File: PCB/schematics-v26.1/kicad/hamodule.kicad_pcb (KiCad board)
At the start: 4 copper layers, 131.1 x 83.7 mm, 206 parts, among them J1 GND|5V, J10 Tx|Rx, J11 Sda|Scl, J12 3|9, J13 13|12, J14 3.3v|GND|7|15, J15 2604-1104, J16 2604-1104, J17 TestPoint, J19 TestPoint, J2 2604-1102, J3 USB_C_Receptacle_USB2.0, J4 GND|3.3V, J5 Jumper 3.3v, J6 2604-1104, J7 2604-1104, J8 5v|GND|Do, J9 Screen, K1 AQG22205, K2 AQG22205, K3 AQG22205, K4 AQG22205, K5 AQG22205, K6 AQG22205, K7 AQG22205, K8 AQG22205, SW1 USB | PS, SW2 Reset, SW3 Boot, U1 LD1117AV33, U10 SN74LV1T34DBV, U11 ULN2803A, U12 TCAL6416, U14 74AHC1G04, U2 USBLC6-2SC6, U3 ESP32-S3-WROOM-2, U4 LDA210, U5 LDA210, U6 LDA210, U7 LDA210, U8 SHT4x, U9 SN74LVCH8T245

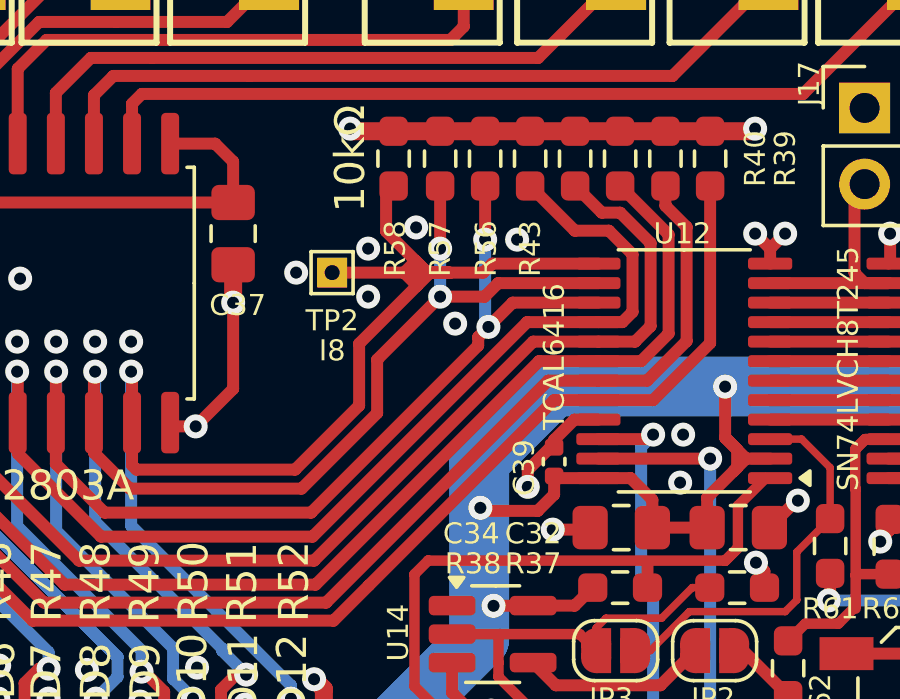
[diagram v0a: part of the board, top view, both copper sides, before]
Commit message: moved a bit the data lines between TCAL and SNT to make sure they have solid GND plane beneath. Updated footprints from library since Kibot complains. lets see if it fixes it
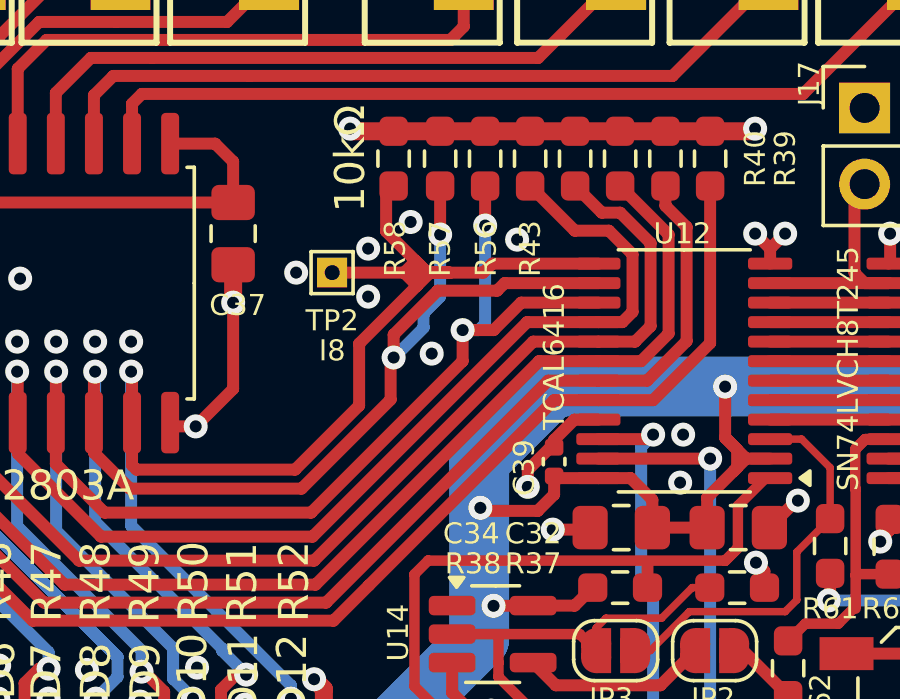
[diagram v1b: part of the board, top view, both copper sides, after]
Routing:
- net Net-(U11-I7): track 43.0 -> 45.8 mm
- net Net-(U11-I6): track 43.6 -> 44.7 mm
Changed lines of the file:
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@@
 		(tags "CP Radial series Radial pin pitch 2.50mm diameter 6.3mm height 7mm Electrolytic Capacitor")
 		(property "Reference" "C12"
-			(at 4.582379 2.6 180)
+			(at 4.582379 2.6 0)
 			(layer "F.SilkS")
 			(effects
@@
 	)
 	(via
-		(at 75.2 86.294307)
+		(at 75.017347 86.111653)
 		(size 0.8)
 		(drill 0.4)
@@
 	)
 	(via
-		(at 76.5 89.5)
+		(at 75.719269 90.499269)
 		(size 0.8)
 		(drill 0.4)
@@
 	)
 	(segment
+		(start 78.15 88.15)
+		(end 81.275 88.15)
+		(width 0.4)
+		(layer "F.Cu")
+		(net 168)
+	)
+	(segment
 		(start 64.46 92.8)
 		(end 64.46 91.14)
@@
 	)
 	(segment
-		(start 73.901 92.481786)
-		(end 71.382786 95)
+		(start 75.916156 88.402)
+		(end 77.898 88.402)
 		(width 0.4)
 		(layer "F.Cu")
@@
 	)
 	(segment
-		(start 64.46 93.799999)
-		(end 64.46 92.925)
+		(start 65.660001 95)
+		(end 64.46 93.799999)
 		(width 0.4)
 		(layer "F.Cu")
@@
 	)
 	(segment
-		(start 76 87)
-		(end 76 84.9125)
+		(start 69.199395 101.200605)
+		(end 69.533773 101.200605)
 		(width 0.4)
 		(layer "F.Cu")
@@
 	)
 	(segment
-		(start 77.935784 88.15)
-		(end 81.275 88.15)
+		(start 64.46 93.799999)
+		(end 64.46 92.925)
 		(width 0.4)
 		(layer "F.Cu")
@@
 	)
 	(segment
-		(start 76 88.601)
-		(end 73.901 90.7)
+		(start 74.45 90.63)
+		(end 74.45 89.868156)
 		(width 0.4)
 		(layer "F.Cu")
@@
 	)
 	(segment
-		(start 69.199395 101.200605)
-		(end 69.533773 101.200605)
+		(start 68.698 101.702)
+		(end 69.199395 101.200605)
 		(width 0.4)
 		(layer "F.Cu")
@@
 	)
 	(segment
-		(start 77.484784 88.601)
-		(end 77.935784 88.15)
+		(start 74.45 89.868156)
+		(end 75.916156 88.402)
 		(width 0.4)
 		(layer "F.Cu")
@@
 	)
 	(segment
-		(start 68.698 101.702)
-		(end 69.199395 101.200605)
+		(start 68.698 102.974004)
+		(end 68.698 101.702)
 		(width 0.4)
 		(layer "F.Cu")
@@
 	)
 	(segment
-		(start 65.660001 95)
-		(end 64.46 93.799999)
+		(start 69.4 103.676004)
+		(end 68.698 102.974004)
 		(width 0.4)
 		(layer "F.Cu")
@@
 	)
 	(segment
-		(start 68.698 102.974004)
-		(end 68.698 101.702)
+		(start 74.35 92.032786)
+		(end 71.382786 95)
 		(width 0.4)
 		(layer "F.Cu")
@@
 	)
 	(segment
-		(start 69.4 103.676004)
-		(end 68.698 102.974004)
+		(start 74.45 90.63)
+		(end 74.35 90.73)
 		(width 0.4)
 		(layer "F.Cu")
@@
 	)
 	(segment
-		(start 73.901 90.7)
-		(end 73.901 92.481786)
+		(start 76 86.53)
+		(end 76 84.9125)
 		(width 0.4)
 		(layer "F.Cu")
@@
 	)
 	(segment
-		(start 76 88.601)
-		(end 77.484784 88.601)
+		(start 74.35 90.73)
+		(end 74.35 92.032786)
 		(width 0.4)
 		(layer "F.Cu")
@@
 	)
 	(segment
-		(start 71.382786 95)
-		(end 65.660001 95)
+		(start 77.898 88.402)
+		(end 78.15 88.15)
 		(width 0.4)
 		(layer "F.Cu")
@@
 		(net 168)
 	)
+	(segment
+		(start 71.382786 95)
+		(end 65.660001 95)
+		(width 0.4)
+		(layer "F.Cu")
+		(net 168)
+	)
 	(via
 		(at 64.5 91.1)
@@
 	)
 	(via
-		(at 76 87)
+		(at 76 86.53)
 		(size 0.8)
 		(drill 0.4)
@@
 	)
 	(via
-		(at 76 88.601)
+		(at 74.45 90.63)
 		(size 0.8)
 		(drill 0.4)
@@
 	)
 	(segment
-		(start 76 88.601)
-		(end 76 87)
+		(start 68.731478 100.331478)
+		(end 64.5 96.1)
 		(width 0.4)
 		(layer "B.Cu")
@@
 	)
 	(segment
-		(start 68.731478 100.331478)
-		(end 64.5 96.1)
+		(start 74.457166 90.63)
+		(end 75.45 89.637166)
 		(width 0.4)
 		(layer "B.Cu")
@@
 	)
 	(segment
+		(start 75.45 89.637166)
+		(end 75.45 89.151)
+		(width 0.4)
+		(layer "B.Cu")
+		(net 168)
+	)
+	(segment
 		(start 64.5 96.1)
 		(end 64.5 91.1)
@@
 	)
 	(segment
-		(start 78.41857 88.8)
-		(end 81.275 88.8)
+		(start 74.45 90.63)
+		(end 74.457166 90.63)
+		(width 0.4)
+		(layer "B.Cu")
+		(net 168)
+	)
+	(segment
+		(start 76 88.601)
+		(end 76 86.53)
+		(width 0.4)
+		(layer "B.Cu")
+		(net 168)
+	)
+	(segment
+		(start 75.45 89.151)
+		(end 76 88.601)
+		(width 0.4)
+		(layer "B.Cu")
+		(net 168)
+	)
+	(segment
+		(start 63.19 94.174999)
+		(end 63.19 93.3)
 		(width 0.4)
 		(layer "F.Cu")
@@
 	)
 	(segment
-		(start 67.763 103.664604)
-		(end 67.7744 103.676004)
+		(start 76.75 89.715711)
+		(end 77.784289 89.715711)
 		(width 0.4)
 		(layer "F.Cu")
@@
 	)
 	(segment
-		(start 77.609285 89.609285)
-		(end 78.41857 88.8)
+		(start 71.7 95.8)
+		(end 64.815001 95.8)
 		(width 0.4)
 		(layer "F.Cu")
@@
 	)
 	(segment
-		(start 63.19 91.11)
-		(end 63.2 91.1)
+		(start 76.75 89.715711)
+		(end 76.75 90.75)
 		(width 0.4)
 		(layer "F.Cu")
@@
 	)
 	(segment
-		(start 64.815001 95.8)
-		(end 63.19 94.174999)
+		(start 77.784289 89.715711)
+		(end 78.7 88.8)
 		(width 0.4)
 		(layer "F.Cu")
@@
 	)
 	(segment
-		(start 63.19 94.174999)
-		(end 63.19 93.3)
+		(start 67.763 103.664604)
+		(end 67.7744 103.676004)
 		(width 0.4)
 		(layer "F.Cu")
@@
 	)
 	(segment
-		(start 71.7 95.8)
-		(end 64.815001 95.8)
+		(start 78.7 88.8)
+		(end 81.275 88.8)
 		(width 0.4)
 		(layer "F.Cu")
@@
 	)
 	(segment
-		(start 77.268426 89.950144)
-		(end 77.268426 90.231574)
+		(start 63.19 91.11)
+		(end 63.2 91.1)
 		(width 0.4)
 		(layer "F.Cu")
@@
 	)
 	(segment
-		(start 77.268426 90.231574)
-		(end 71.7 95.8)
+		(start 77.5 86.23)
+		(end 77.5 84.9125)
 		(width 0.4)
 		(layer "F.Cu")
@@
 	)
 	(segment
-		(start 77.5 86.7)
-		(end 77.5 84.9125)
+		(start 63.19 92.8)
+		(end 63.19 91.11)
 		(width 0.4)
 		(layer "F.Cu")
@@
 	)
 	(segment
-		(start 63.19 92.8)
-		(end 63.19 91.11)
+		(start 64.815001 95.8)
+		(end 63.19 94.174999)
 		(width 0.4)
 		(layer "F.Cu")
@@
 	)
 	(segment
-		(start 77.609285 89.609285)
-		(end 77.268426 89.950144)
+		(start 76.75 90.75)
+		(end 71.7 95.8)
 		(width 0.4)
 		(layer "F.Cu")
@@
 	)
 	(via
-		(at 77.609285 89.609285)
+		(at 76.75 89.715711)
 		(size 0.8)
 		(drill 0.4)
@@
 	)
 	(via
-		(at 77.5 86.7)
+		(at 77.5 86.23)
 		(size 0.8)
 		(drill 0.4)
@@
 	)
 	(segment
-		(start 67.098 100.316414)
-		(end 67.098 101.335)
+		(start 77.5 89.5)
+		(end 77.5 86.23)
 		(width 0.4)
 		(layer "B.Cu")
@@
 	)
 	(segment
-		(start 77.5 89.5)
-		(end 77.609285 89.609285)
+		(start 67.098 100.316414)
+		(end 67.098 101.335)
 		(width 0.4)
 		(layer "B.Cu")
@@
 	)
 	(segment
+		(start 76.75 89.715711)
+		(end 77.284289 89.715711)
+		(width 0.4)
+		(layer "B.Cu")
+		(net 169)
+	)
+	(segment
 		(start 65.840793 99.059207)
 		(end 67.098 100.316414)
@@
 	)
 	(segment
-		(start 77.5 86.7)
+		(start 77.284289 89.715711)
 		(end 77.5 89.5)
 		(width 0.4)

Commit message: Finished Size 1
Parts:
- moved H5 0.83 mm to (52.2, 104.6)
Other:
- board size 131.1 x 83.7 mm -> 131.9 x 84.5 mm
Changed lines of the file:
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@@
 	(footprint "MountingHole:MountingHole_3.2mm_M3_ISO14580_Pad"
 		(layer "F.Cu")
-		(at 52.25 103.8)
+		(at 52.25 104.63)
 		(descr "Mounting Hole 3.2mm, M3, generated by kicad-footprint-generator mountinghole.py")
 		(tags "mountinghole M3 ISO14580")
@@
 	)
 	(gr_line
-		(start 147.25 31.8)
-		(end 31.37071 31.8)
+		(start 147.05 31.03)
+		(end 31.391411 31.03)
 		(stroke
 			(width 0.05)
@@
 	)
 	(gr_line
-		(start 23.9 106.3)
-		(end 23.900001 40.4004)
+		(start 23.05 106.3)
+		(end 23.05 40.4004)
 		(stroke
 			(width 0.05)
@@
 	)
 	(gr_line
-		(start 31.199084 110.009939)
-		(end 31.200916 115.1)
+		(start 31.1518 109.900032)
+		(end 31.15 115.1)
 		(stroke
 			(width 0.05)
-			(type default)
+			(type solid)
 		)
 		(layer "Edge.Cuts")
 	)
 	(gr_line
-		(start 24.3 40.000401)
-		(end 28.0293 40.001612)
+		(start 23.449999 40.000401)
+		(end 28.048388 40.001617)
 		(stroke
 			(width 0.05)
@@
 	)
 	(gr_arc
-		(start 147.25 31.8)
-		(mid 147.391421 31.858579)
-		(end 147.45 32)
+		(start 147.05 31.03)
+		(mid 147.191421 31.088579)
+		(end 147.25 31.23)
 		(stroke
 			(width 0.05)
@@
 	)
 	(gr_line
-		(start 27.901832 106.600916)
-		(end 24.2 106.6)
+		(start 27.85 106.600916)
+		(end 23.35 106.6)
 		(stroke
 			(width 0.05)
@@
 	)
 	(gr_arc
-		(start 150.65 40)
-		(mid 148.387258 39.062742)
-		(end 147.45 36.8)
+		(start 150.45 40)
+		(mid 148.187258 39.062742)
+		(end 147.25 36.8)
 		(stroke
 			(width 0.05)
@@
 	)
 	(gr_arc
-		(start 23.900001 40.4004)
-		(mid 24.017158 40.117558)
-		(end 24.3 40.000401)
+		(start 23.05 40.4004)
+		(mid 23.167157 40.117558)
+		(end 23.449999 40.000401)
 		(stroke
 			(width 0.05)
@@
 	)
 	(gr_arc
-		(start 31.130912 36.9)
-		(mid 30.222471 39.093171)
-		(end 28.0293 40.001612)
+		(start 31.15 36.9)
+		(mid 30.241559 39.093171)
+		(end 28.048388 40.001612)
 		(stroke
 			(width 0.05)
@@
 	)
 	(gr_line
-		(start 31.13 36.9)
-		(end 31.13 32.0414)
+		(start 31.15 36.9)
+		(end 31.15 31.271411)
 		(stroke
 			(width 0.05)
@@
 	)
 	(gr_line
-		(start 150.65 40)
+		(start 150.45 40)
 		(end 154.8 40)
 		(stroke
@@
 	)
 	(gr_line
-		(start 147.45 36.8)
-		(end 147.45 32)
+		(start 147.25 36.8)
+		(end 147.25 31.23)
 		(stroke
 			(width 0.05)
@@
 	)
 	(gr_arc
-		(start 24.2 106.6)
-		(mid 23.987868 106.512132)
-		(end 23.9 106.3)
+		(start 23.35 106.6)
+		(mid 23.137868 106.512132)
+		(end 23.05 106.3)
 		(stroke
 			(width 0.05)
@@
 	)
 	(gr_arc
-		(start 31.6 115.5)
-		(mid 31.317157 115.382843)
-		(end 31.2 115.1)
+		(start 31.55 115.5)
+		(mid 31.267157 115.382843)
+		(end 31.15 115.1)
 		(stroke
 			(width 0.05)
@@
 	)
 	(gr_arc
-		(start 27.901832 106.600916)
-		(mid 30.273186 107.606395)
-		(end 31.199084 110.009939)
+		(start 27.852748 106.600916)
+		(mid 30.185543 107.567218)
+		(end 31.1518 109.900032)
 		(stroke
 			(width 0.05)
-			(type default)
+			(type solid)
 		)
 		(layer "Edge.Cuts")
@@
 	(gr_line
 		(start 134.0866 115.5)
-		(end 31.6 115.5)
+		(end 31.55 115.5)
 		(stroke
 			(width 0.05)
@@
 	)
 	(gr_arc
-		(start 31.129289 32.0414)
-		(mid 31.199997 31.870697)
-		(end 31.3707 31.799989)
+		(start 31.15 31.271411)
+		(mid 31.220708 31.100708)
+		(end 31.391411 31.03)
 		(stroke
 			(width 0.05)
@@
 		(layer "Dwgs.User")
 		(pts
-			(xy 31.6 115.5) (xy 31.368396 31.8)
+			(xy 31.6 115.5) (xy 31.45 31.03)
 		)
 		(height -17.498728)
@@
 			(keep_text_aligned yes)
 		)
-		(gr_text "83.7003 mm"
-			(at 15.135533 73.695238 -89.84145881)
+		(gr_text "84.4701 mm"
+			(at 15.176298 73.294032 -89.8982555)
 			(layer "Dwgs.User")
 			(effects
@@
 		(layer "Dwgs.User")
 		(pts
-			(xy 147.8 31.8) (xy 147.8 40)
+			(xy 147.05 31.03) (xy 147.05 40.03)
 		)
 		(height -10.5)
@@
 			(keep_text_aligned yes)
 		)
-		(gr_text "8.2000 mm"
-			(at 157.15 35.9 90)
+		(gr_text "9.0000 mm"
+			(at 156.399984 35.529993 90)
 			(layer "Dwgs.User")
 			(effects
@@
 		(layer "Dwgs.User")
 		(pts
-			(xy 23.9 106.6) (xy 23.900001 42.017524)
+			(xy 23.9 106.6) (xy 23.900001 40.03)
 		)
 		(height -3.3)
@@
 			(keep_text_aligned yes)
 		)
-		(gr_text "64.5825 mm"
-			(at 19.450001 74.308762 89.99999823)
+		(gr_text "66.5700 mm"
+			(at 19.450001 73.315 89.99999828)
 			(layer "Dwgs.User")
 			(effects
@@
 		(layer "Dwgs.User")
 		(pts
-			(xy 52.25 115.5) (xy 52.25 103.8)
+			(xy 52.25 115.5) (xy 52.25 104.63)
 		)
-		(height -33.45)
+		(height -33.4)
 		(format
 			(prefix "")
@@
 			(keep_text_aligned yes)
 		)
-		(gr_text "11.7000 mm"
-			(at 17.56215 109.65 90)
+		(gr_text "10.8700 mm"
+			(at 17.61215 110.065 90)
 			(layer "Dwgs.User")
 			(effects
@@
 		(layer "Dwgs.User")
 		(pts
-			(xy 52.25 103.8) (xy 23.9 103.8)
+			(xy 52.25 103.8) (xy 23.05 103.8)
 		)
 		(height -18.7)
@@
 			(keep_text_aligned yes)
 		)
-		(gr_text "28.3500 mm"
-			(at 38.063428 121.806672 0)
+		(gr_text "29.2000 mm"
+			(at 37.638078 121.806672 0)
 			(layer "Dwgs.User")
 			(effects
@@
 		(layer "Dwgs.User")
 		(pts
-			(xy 31.129289 32.4) (xy 147.45 32.4)
+			(xy 31.129289 32.4) (xy 147.25 32.4)
 		)
 		(height -8)
@@
 			(keep_text_aligned yes)
 		)
-		(gr_text "116.3207 mm"
-			(at 89.022321 23.449991 0)
+		(gr_text "116.1207 mm"
+			(at 88.92278 23.449989 0)
 			(layer "Dwgs.User")
 			(effects
@@
 		(layer "Dwgs.User")
 		(pts
-			(xy 147.45 36.8) (xy 155 36.83)
+			(xy 147.25 36.8) (xy 155.05 36.83)
 		)
-		(height -12.302627)
+		(height -12.460317)
 		(format
 			(prefix "")
@@
 			(keep_text_aligned yes)
 		)
-		(gr_text "7.5501 mm"
-			(at 151.278454 23.362479 359.7723358)
+		(gr_text "7.8001 mm"
+			(at 151.202347 23.204784 359.7796327)
 			(layer "Dwgs.User")
 			(effects
@@
 		(polygon
 			(pts
-				(xy 23.876 93.9292) (xy 23.876 115.4684) (xy 136.4112 115.443) (xy 136.4234 86.587) (xy 146.248 86.587)
+				(xy 23.076 93.930322) (xy 23.076 115.468581) (xy 136.4112 115.443) (xy 136.4234 86.587) (xy 146.248 86.587)
 				(xy 146.248 79.170351) (xy 119.7322 79.2472) (xy 106.7243 79.2849) (xy 94.85 79.25) (xy 93.7032 71.0422)
 				(xy 44.6786 70.9422) (xy 44.7 93.9)

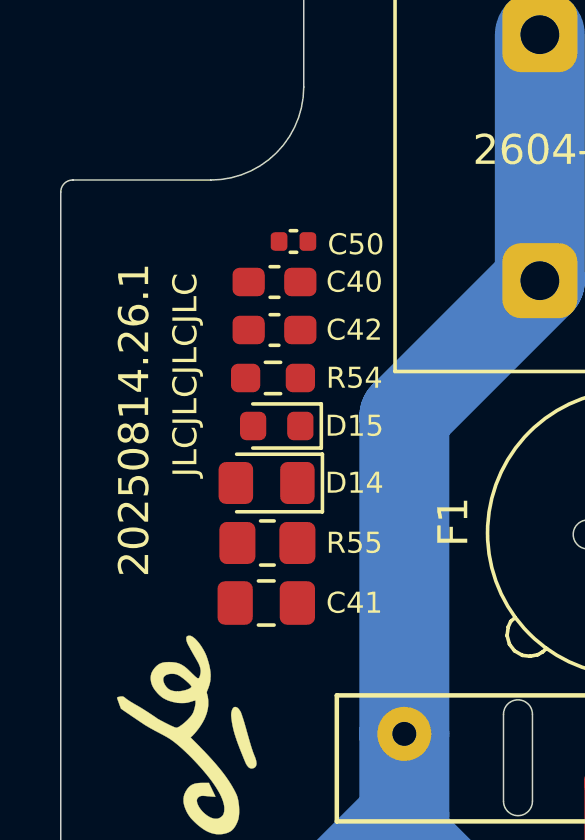
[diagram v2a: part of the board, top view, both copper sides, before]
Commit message: Adding 26 2L. This is a version used only to test fit of the PCB on the case. All v26 will be like that. The main difference is the production files
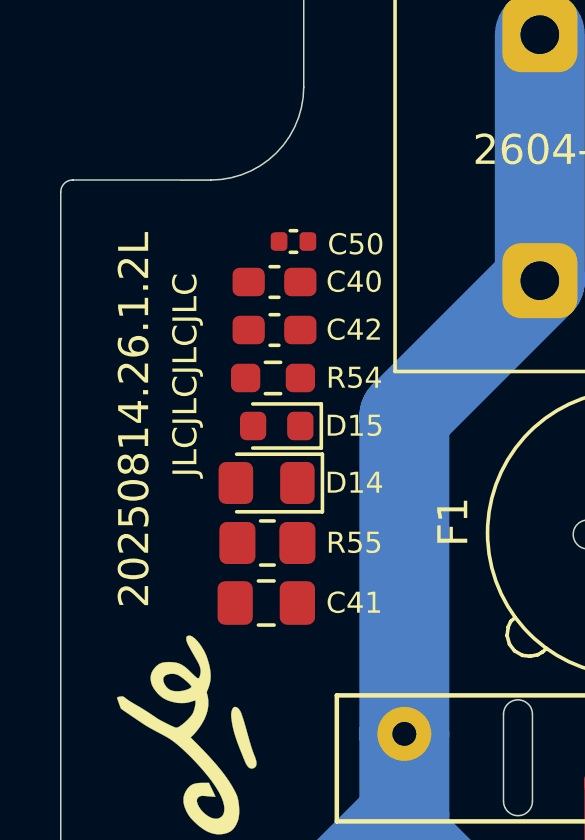
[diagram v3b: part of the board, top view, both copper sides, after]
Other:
- board text added: "20250814.26.1.2L"
- board text removed: "20250814.26.1"
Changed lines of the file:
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@@
 	(title_block
 		(title "Home Assistant module for lights control")
-		(date "2025-08-14")
-		(rev "20250814.26.1")
+		(date "2025-08-19")
+		(rev "20250819.26.1")
 		(comment 1 "https://docs.rs-online.com/e49b/0900766b816e00ad.pdf")
 		(comment 2 "https://media.distrelec.com/Web/Downloads/_t/ds/1862291_eng_tds.pdf")
@@
 			(crossoutdnponfab yes)
 			(subtractmaskfromsilk yes)
-			(outputformat 5)
+			(outputformat 1)
 			(mirror yes)
 			(drillshape 0)
@@
 		(layer "User.2")
 	)
-	(gr_text "20250814.26.1"
+	(gr_text "20250814.26.1.2L"
 		(locked yes)
 		(at 25.5 48 90)
